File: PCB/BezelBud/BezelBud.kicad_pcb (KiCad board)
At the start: 2 copper layers, 44 x 25.6 mm, 40 parts, among them J1 USB_C_Receptacle_USB2.0_16P, J2 Conn_01x05_Pin, SW1 SW_SPDT, SW2 SW_SPDT, U1 USBLC6-2SC6, U2 STM32G431CBT6, U3 LP5907MFX-3.3, U4 GSA4030H10-B26-5P, Y1 Crystal_GND24

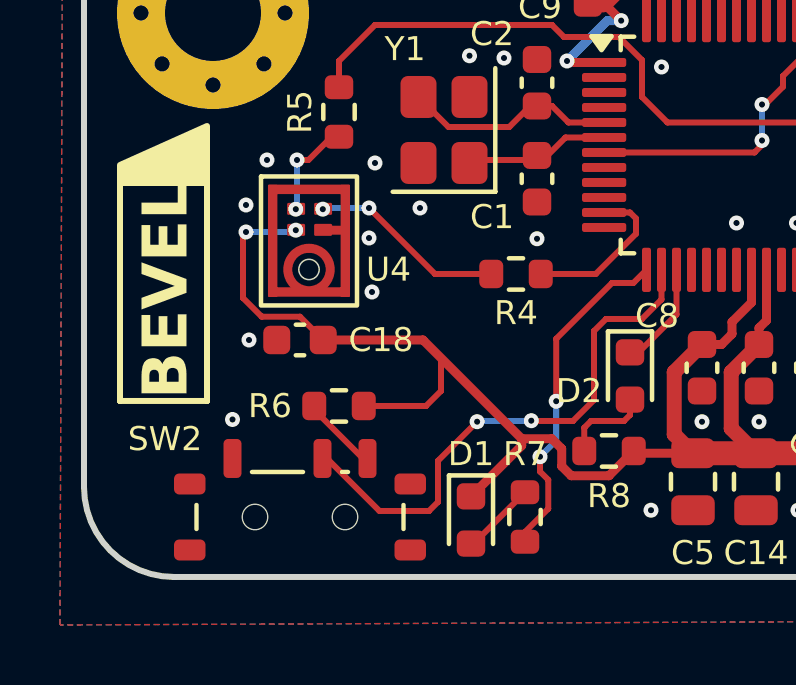
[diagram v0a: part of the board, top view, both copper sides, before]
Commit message: deleted gerbers and fixed LED orientation
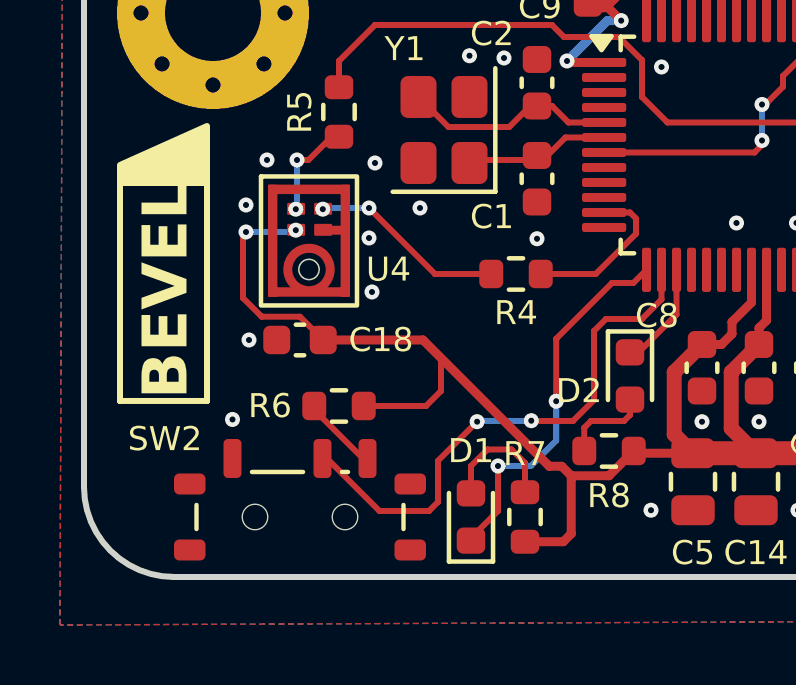
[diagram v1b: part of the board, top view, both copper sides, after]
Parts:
- moved D1 0.10 mm to (147.9, 94.6), turned to 90 degrees
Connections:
- D1 pad 1: +3.3V -> /LED_LIVE
- R7 pad 1: /LED_LIVE -> +3.3V
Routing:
- net /R_A: track 2.51 -> 4.10 mm
- net /LED_LIVE: track 11.4 -> 12.5 mm
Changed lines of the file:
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@@
 			(layers "F.Cu" "F.Mask" "F.Paste")
 			(roundrect_rratio 0.25)
-			(net 9 "/LED_LIVE")
+			(net 2 "+3.3V")
 			(pintype "passive")
 		)
@@
 	(footprint "LED_SMD:LED_0603_1608Metric"
 		(layer "F.Cu")
-		(at 147.9 94.7 -90)
+		(at 147.9 94.6 90)
 		(descr "LED SMD 0603 (1608 Metric), square (rectangular) end terminal, IPC-7351 nominal, (Body size source: http://www.tortai-tech.com/upload/download/2011102023233369053.pdf), generated with kicad-footprint-generator")
 		(tags "LED")
 		(property "Reference" "D1"
-			(at -2.2 0 0)
+			(at 2.2 0 0)
 			(unlocked yes)
 			(layer "F.SilkS")
@@
 		)
 		(property "Value" "LED"
-			(at 0 1.43 270)
+			(at 0 1.43 90)
 			(unlocked yes)
 			(layer "F.Fab")
@@
 		)
 		(property "Datasheet" "~"
-			(at 0 0 270)
+			(at 0 0 90)
 			(unlocked yes)
 			(layer "F.Fab")
@@
 		)
 		(property "Description" "Light emitting diode"
-			(at 0 0 270)
+			(at 0 0 90)
 			(unlocked yes)
 			(layer "F.Fab")
@@
 		)
 		(property "Sim.Pins" "1=K 2=A"
-			(at 0 0 270)
+			(at 0 0 90)
 			(unlocked yes)
 			(layer "F.Fab")
@@
 		)
 		(property "Colour" "Red"
-			(at 0 0 270)
+			(at 0 0 90)
 			(unlocked yes)
 			(layer "F.Fab")
@@
 		(attr smd)
 		(fp_line
-			(start -1.485 0.735)
-			(end 0.8 0.735)
+			(start 0.8 -0.735)
+			(end -1.485 -0.735)
 			(stroke
 				(width 0.15)
@@
 		)
 		(fp_line
-			(start 0.8 -0.735)
-			(end -1.485 -0.735)
+			(start -1.485 0.735)
+			(end 0.8 0.735)
 			(stroke
 				(width 0.15)
@@
 		)
 		(fp_line
-			(start -0.8 0.4)
-			(end 0.8 0.4)
+			(start 0.8 -0.4)
+			(end -0.5 -0.4)
 			(stroke
 				(width 0.2)
@@
 		)
 		(fp_line
-			(start 0.8 0.4)
-			(end 0.8 -0.4)
+			(start -0.5 -0.4)
+			(end -0.8 -0.1)
 			(stroke
 				(width 0.2)
@@
 		)
 		(fp_line
-			(start -0.5 -0.4)
-			(end -0.8 -0.1)
+			(start 0.8 0.4)
+			(end 0.8 -0.4)
 			(stroke
 				(width 0.2)
@@
 		)
 		(fp_line
-			(start 0.8 -0.4)
-			(end -0.5 -0.4)
+			(start -0.8 0.4)
+			(end 0.8 0.4)
 			(stroke
 				(width 0.2)
@@
 		)
 		(fp_text user "${REFERENCE}"
-			(at 0 0 270)
+			(at 0 0 90)
 			(unlocked yes)
 			(layer "F.Fab")
@@
 		)
 		(pad "1" smd roundrect
-			(at -0.7875 0 270)
+			(at -0.7875 0 90)
 			(size 0.875 0.95)
 			(layers "F.Cu" "F.Mask" "F.Paste")
 			(roundrect_rratio 0.25)
-			(net 2 "+3.3V")
+			(net 9 "/LED_LIVE")
 			(pinfunction "K")
 			(pintype "passive")
 		)
 		(pad "2" smd roundrect
-			(at 0.7875 0 270)
+			(at 0.7875 0 90)
 			(size 0.875 0.95)
 			(layers "F.Cu" "F.Mask" "F.Paste")
@@
 	)
 	(gr_rect
-		(start 136.2 90.732785)
-		(end 139.1 83.467215)
+		(start 136.2 83.467215)
+		(end 139.1 90.732785)
 		(stroke
 			(width 0.2)
@@
 	)
 	(segment
+		(start 151.241226 95.158774)
+		(end 150.975 95.425)
+		(width 0.3)
+		(layer "F.Cu")
+		(net 2)
+	)
+	(segment
 		(start 161.75 93.35)
 		(end 160.35 93.35)
@@
 	)
 	(segment
-		(start 152.9 76.1)
-		(end 153.325 75.675)
-		(width 0.6)
+		(start 150.924 92.908774)
+		(end 150.508774 92.908774)
+		(width 0.3)
 		(layer "F.Cu")
 		(net 2)
 	)
 	(segment
-		(start 149.59138 92.22112)
-		(end 147.9 93.9125)
-		(width 0.3)
+		(start 152.9 76.1)
+		(end 153.325 75.675)
+		(width 0.6)
 		(layer "F.Cu")
 		(net 2)
@@
 	)
 	(segment
-		(start 150.924 92.908774)
-		(end 150.924 92.324)
+		(start 146.3 88.7)
+		(end 142.975 88.7)
 		(width 0.3)
 		(layer "F.Cu")
@@
 	)
 	(segment
-		(start 160.675 77.575)
-		(end 160.1 77)
-		(width 0.8)
+		(start 150.975 95.425)
+		(end 150.151 95.425)
+		(width 0.3)
 		(layer "F.Cu")
 		(net 2)
 	)
 	(segment
-		(start 157.75 88.05)
-		(end 157.75 86.3625)
+		(start 151.241226 93.226)
+		(end 151.241226 95.158774)
 		(width 0.3)
 		(layer "F.Cu")
@@
 	)
 	(segment
-		(start 156.25 88.85)
-		(end 156.6 88.5)
-		(width 0.3)
+		(start 160.675 77.575)
+		(end 160.1 77)
+		(width 0.8)
 		(layer "F.Cu")
 		(net 2)
 	)
 	(segment
-		(start 150.924 92.324)
-		(end 150.59138 91.99138)
+		(start 157.75 88.05)
+		(end 157.75 86.3625)
 		(width 0.3)
 		(layer "F.Cu")
@@
 	)
 	(segment
-		(start 152.325896 77.475)
-		(end 151.8 77.475)
+		(start 156.25 88.85)
+		(end 156.6 88.5)
 		(width 0.3)
 		(layer "F.Cu")
@@
 	)
 	(segment
-		(start 150.59138 91.99138)
-		(end 149.59138 91.99138)
+		(start 152.325896 77.475)
+		(end 151.8 77.475)
 		(width 0.3)
 		(layer "F.Cu")
@@
 	)
 	(segment
+		(start 151.241226 93.226)
+		(end 150.924 92.908774)
+		(width 0.3)
+		(layer "F.Cu")
+		(net 2)
+	)
+	(segment
 		(start 159.375 75.675)
 		(end 157.4 75.675)
@@
 	)
 	(segment
-		(start 151.241226 93.226)
-		(end 150.924 92.908774)
-		(width 0.3)
-		(layer "F.Cu")
-		(net 2)
-	)
-	(segment
 		(start 152.425 73.825)
 		(end 151.8 73.825)
@@
 	)
 	(segment
-		(start 146.3 88.7)
-		(end 142.975 88.7)
+		(start 150.508774 92.908774)
+		(end 146.3 88.7)
 		(width 0.3)
 		(layer "F.Cu")
@@
 	)
 	(segment
-		(start 149.59138 91.99138)
-		(end 146.3 88.7)
-		(width 0.3)
-		(layer "F.Cu")
-		(net 2)
-	)
-	(segment
 		(start 159.9 92.3)
 		(end 159.725 92.475)
@@
 	)
 	(segment
-		(start 149.59138 91.99138)
-		(end 149.59138 92.22112)
-		(width 0.3)
-		(layer "F.Cu")
-		(net 2)
-	)
-	(segment
 		(start 157.46 75.615)
 		(end 157.4 75.675)
@@
 	)
 	(segment
-		(start 150.2 92.59138)
-		(end 150.2 93.085936)
-		(width 0.2)
-		(layer "F.Cu")
-		(net 9)
-	)
-	(segment
-		(start 150.2 93.085936)
-		(end 150.476 93.361936)
-		(width 0.2)
-		(layer "F.Cu")
-		(net 9)
-	)
-	(segment
 		(start 152.6 86.8)
 		(end 153.3125 86.8)
@@
 	)
 	(segment
-		(start 150.476 94.324)
-		(end 149.7 95.1)
+		(start 153.3125 86.8)
+		(end 153.75 86.3625)
 		(width 0.2)
 		(layer "F.Cu")
@@
 	)
 	(segment
-		(start 153.3125 86.8)
-		(end 153.75 86.3625)
+		(start 147.9 95.3875)
+		(end 147.9 95.3)
 		(width 0.2)
 		(layer "F.Cu")
@@
 	)
 	(segment
-		(start 150.476 93.361936)
-		(end 150.476 94.324)
+		(start 147.9 95.3)
+		(end 148.8 94.4)
 		(width 0.2)
 		(layer "F.Cu")
@@
 	)
 	(segment
-		(start 150.74038 90.74038)
-		(end 150.74038 88.65962)
+		(start 148.8 94.4)
+		(end 148.8 92.9)
 		(width 0.2)
 		(layer "F.Cu")
@@
 	)
 	(segment
-		(start 149.7 95.1)
-		(end 149.7 95.425)
+		(start 150.74038 90.74038)
+		(end 150.74038 88.65962)
 		(width 0.2)
 		(layer "F.Cu")
@@
 	)
 	(via
-		(at 150.2 92.59138)
+		(at 148.8 92.9)
 		(size 0.5)
 		(drill 0.2)
@@
 	)
 	(segment
-		(start 150.74038 90.74038)
+		(start 149.89138 92.9)
 		(end 150.74038 92.051)
 		(width 0.2)
@@
 	)
 	(segment
+		(start 148.8 92.9)
+		(end 149.89138 92.9)
+		(width 0.2)
+		(layer "B.Cu")
+		(net 9)
+	)
+	(segment
 		(start 150.74038 92.051)
-		(end 150.2 92.59138)
+		(end 150.74038 90.74038)
 		(width 0.2)
 		(layer "B.Cu")
@@
 	)
 	(segment
-		(start 147.9 95.4875)
-		(end 147.9875 95.4875)
+		(start 149.7 92.8)
+		(end 149.7 93.775)
 		(width 0.2)
 		(layer "F.Cu")
@@
 	)
 	(segment
-		(start 147.9875 95.4875)
-		(end 149.7 93.775)
+		(start 148.451 92.349)
+		(end 149.249 92.349)
+		(width 0.2)
+		(layer "F.Cu")
+		(net 52)
+	)
+	(segment
+		(start 149.249 92.349)
+		(end 149.7 92.8)
+		(width 0.2)
+		(layer "F.Cu")
+		(net 52)
+	)
+	(segment
+		(start 147.9 92.9)
+		(end 148.451 92.349)
+		(width 0.2)
+		(layer "F.Cu")
+		(net 52)
+	)
+	(segment
+		(start 147.9 93.8125)
+		(end 147.9 92.9)
 		(width 0.2)
 		(layer "F.Cu")

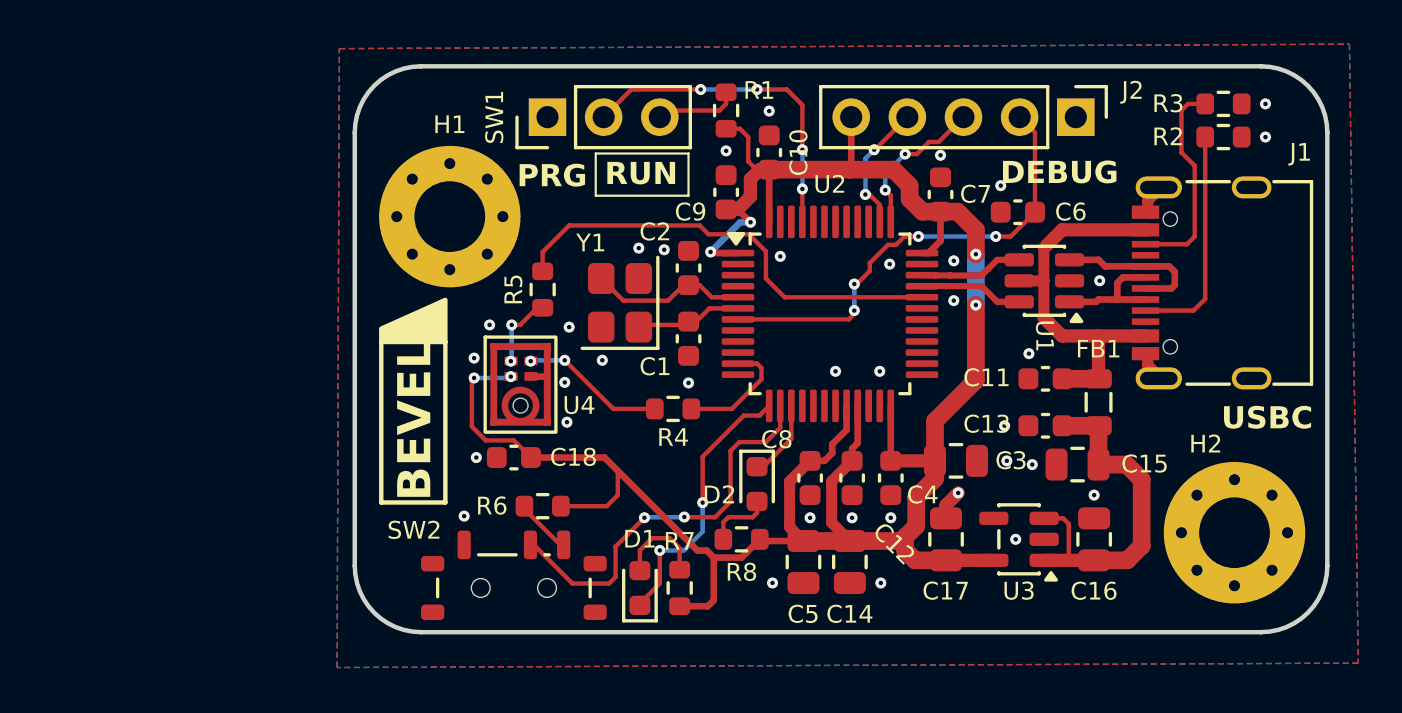
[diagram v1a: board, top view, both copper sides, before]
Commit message: updated footprints for mic and debug
started pcb layout
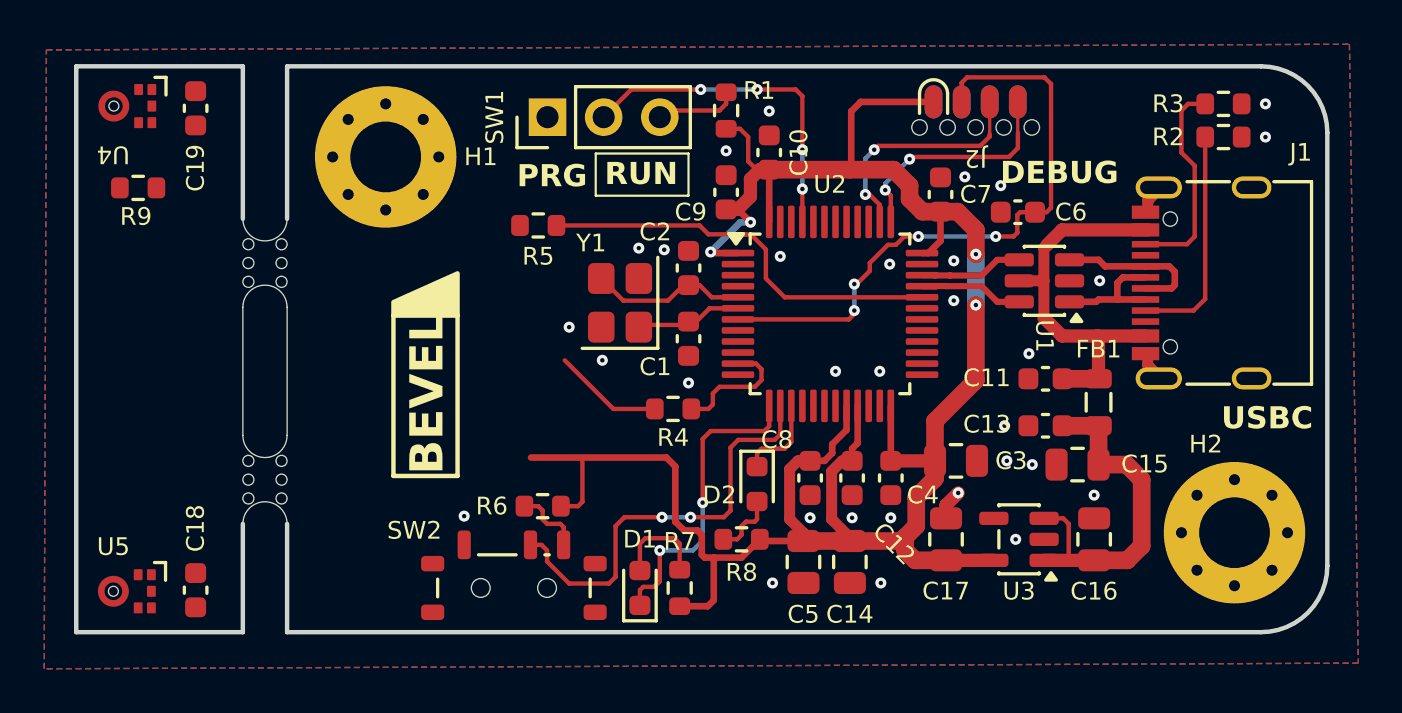
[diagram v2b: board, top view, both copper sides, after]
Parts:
- added C19: 0.1uF, Capacitor_SMD:C_0603_1608Metric, F.Cu at (127.8, 72.9)
- added R9: 10K, Resistor_SMD:R_0603_1608Metric, F.Cu at (125.2, 76.5)
- added REF**: MouseBite-Slot_2.0x2.0mm_outset_D0.5mm_P0.85mm_3h, Panelization:MouseBite-Slot_2.0x2.0mm_outset_D0.5mm_P0.85mm_3h, F.Cu at (131.9, 89.7)
- added REF**: MouseBite-Slot_2.0x2.0mm_outset_D0.5mm_P0.85mm_3h, Panelization:MouseBite-Slot_2.0x2.0mm_outset_D0.5mm_P0.85mm_3h, F.Cu at (131.9, 79.9)
- added U5: MD-LRA371-H20, BevelBud:MD-LRA371-H20, F.Cu at (124.1, 94.8)
- J2: value Conn_01x05_Pin -> SOIC clip_prog; footprint Connector_PinHeader_2.54mm:PinHeader_1x05_P2.54mm_Vertical -> BevelBud:SOIC_clipProgSmall
- U4: value GSA4030H10-B26-5P -> MD-LRA371-H20; footprint BevelBud:GSA4030H10-B26-5P -> BevelBud:MD-LRA371-H20
- moved U4 22.9 mm to (124.1, 72.8), turned to -90 degrees
- moved C18 15.6 mm to (127.8, 94.7), turned to 90 degrees
- moved J2 4.75 mm to (163.1, 71.9), turned to 180 degrees
- moved H1 3.96 mm to (136.4, 75.1)
- moved R5 2.91 mm to (143.3, 78.2), turned to 180 degrees
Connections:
- J2 pad 1: GND -> +3.3V
- J2 pad 3: /SWDIO -> /SWLCK
- J2 pad 4: /SWLCK -> /SWDIO
- J2 pad 5: +3.3V -> unconnected-(J2-Pin_5-Pad5)
- U4 pad 1: +3.3V -> /SAI1_DATA
- U4 pad 2: /MIC2_DATA_TERM -> Net-(U4-L/R)
- U4 pad 3: /SAI1_CLK -> GND
- U4 pad 4: GND -> /SAI1_CLK
- U4 pad 5: GND -> +3.3V
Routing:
- net /NRST: track 21.0 -> 28.5 mm
- net /SWLCK: track 5.92 -> 10.8 mm
- net /SWDIO: track 6.88 -> 10.6 mm
- net /MIC2_DATA_TERM: track 3.38 -> 0.00 mm, vias 2 -> 0
- net /SAI1_DATA: track 20.6 -> 18.7 mm
- net /SAI1_CLK: track 6.54 -> 4.99 mm, vias 2 -> 0
- net /LED_LIVE: track 12.5 -> 14.0 mm
- net /MUTE_SW: track 18.1 -> 19.4 mm
- net +3.3V: track 102.2 -> 100.9 mm, vias 6 -> 4
- net GND: track 4.81 -> 4.11 mm, vias 36 -> 31
- net /SW_H: track 2.64 -> 3.33 mm
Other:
- board size 44 x 25.6 mm -> 56.6 x 25.6 mm

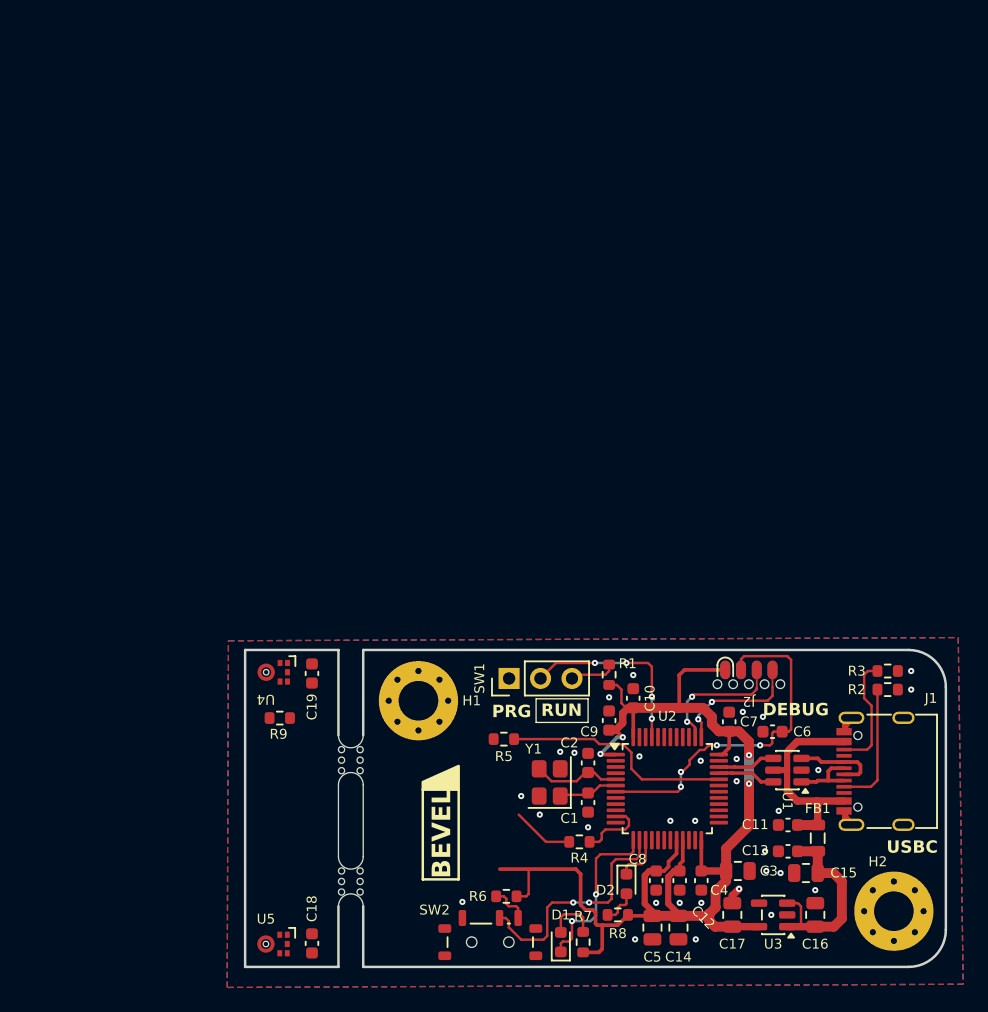
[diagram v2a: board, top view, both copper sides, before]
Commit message: Starting layout for scored and mouse bite PCB
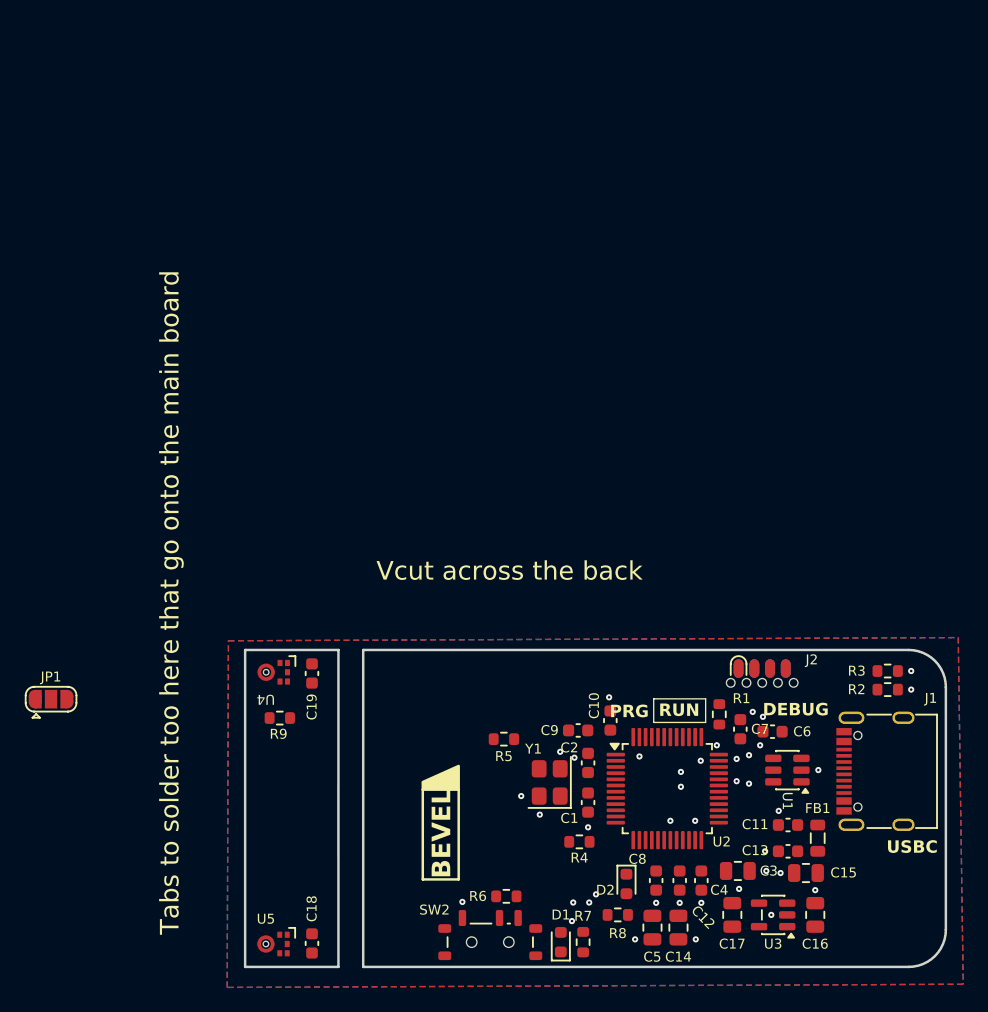
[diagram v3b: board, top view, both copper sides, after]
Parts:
- removed H1, H2: MountingHole_Pad, MountingHole:MountingHole_3.2mm_M3_Pad_Via
- removed REF** (x2): MouseBite-Slot_2.0x2.0mm_outset_D0.5mm_P0.85mm_3h, Panelization:MouseBite-Slot_2.0x2.0mm_outset_D0.5mm_P0.85mm_3h
- removed SW1: SW_SPDT, Connector_PinHeader_2.54mm:PinHeader_1x03_P2.54mm_Vertical
- added JP1: Jumper_3_Bridged12, Jumper:SolderJumper-3_P1.3mm_Open_RoundedPad1.0x1.5mm, F.Cu at (106.7, 75.0)
- moved R1 9.46 mm to (160.7, 76.2)
- moved C9 2.62 mm to (149.3, 77.5), turned to 180 degrees
- moved C10 2.58 mm to (151.9, 76.7)
- moved C7 1.08 mm to (162.4, 77.4)
- moved J2 1.08 mm to (164.2, 71.8)
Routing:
- net +3.3V: track 100.9 -> 0.00 mm, vias 4 -> 2
- net /NRST: track 28.5 -> 0.00 mm
- net /MUTE_SW: track 19.4 -> 0.00 mm
- net /SAI1_DATA: track 18.7 -> 0.00 mm
- net VCC: track 17.8 -> 0.00 mm
- net +5V: track 16.1 -> 0.00 mm
- net /BOOT0: track 15.1 -> 0.00 mm, vias 4 -> 0
- net /LED_LIVE: track 14.0 -> 0.00 mm
- net /SWLCK: track 10.8 -> 0.00 mm, vias 2 -> 0
- net /SWDIO: track 10.6 -> 0.00 mm, vias 2 -> 0
- net /CC1: track 10.2 -> 0.00 mm
- net /CC2: track 9.52 -> 0.00 mm
- net PF0: track 7.12 -> 0.00 mm
- net /USBC_P: track 6.98 -> 0.00 mm
- net /SAI1_CLK_TERM: track 5.67 -> 0.00 mm
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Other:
- outline, holes or cut-outs redrawn
- board text added: "Tabs to solder too here that go onto the main board"
- board text added: "Vcut across the back"
